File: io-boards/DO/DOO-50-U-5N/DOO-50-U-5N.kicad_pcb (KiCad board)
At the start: 2 copper layers, 50 x 33 mm, 17 parts, among them J1 GPP_Conn_01x12_Pin, J3 Conn_01x02_Socket, J4 Conn_01x02_Socket, Q1 NDT3055L, Q2 BC807, U1 PC817

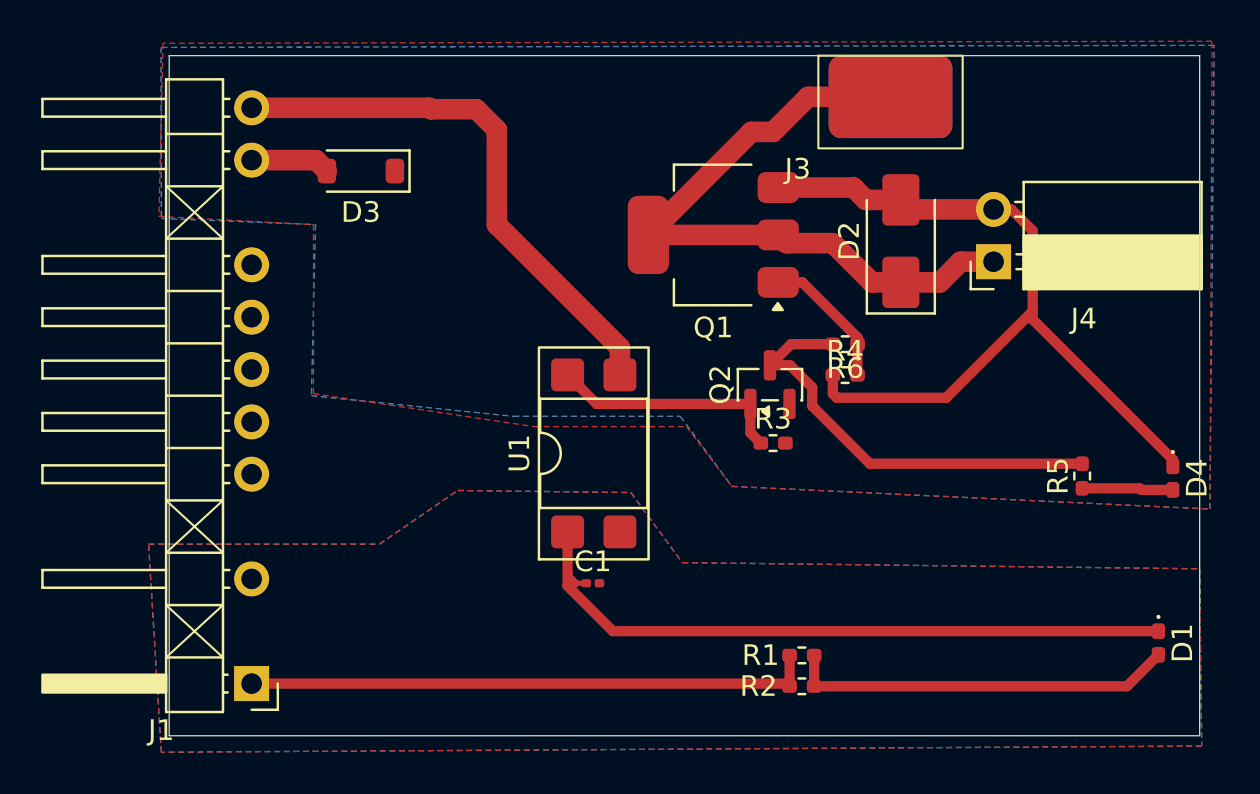
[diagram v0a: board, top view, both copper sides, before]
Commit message: Made some corrections after assembling of prototype PCBs
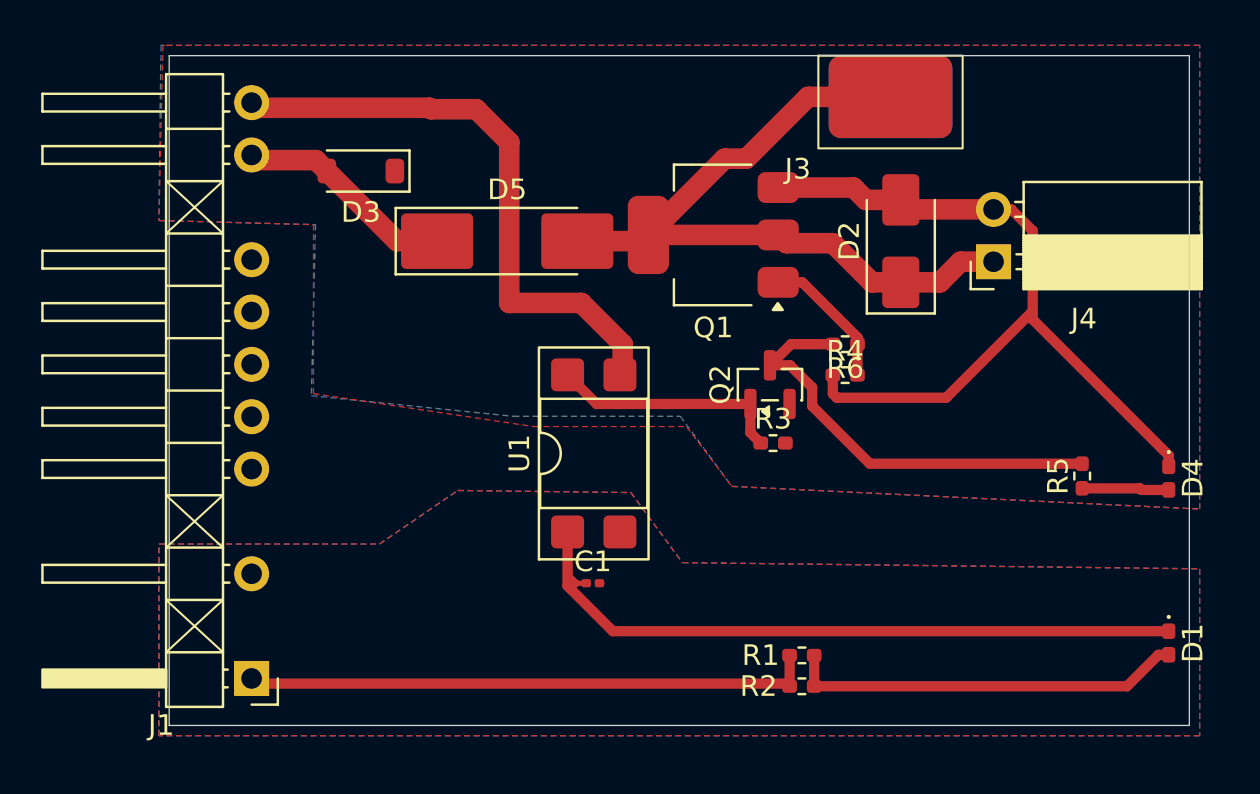
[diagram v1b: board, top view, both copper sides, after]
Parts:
- added D5: SM4007, Diode_SMD:D_MELF_Handsoldering, F.Cu at (116.4, 59.0)
- moved D1 0.50 mm to (148.5, 78.5)
- moved J1 0.25 mm to (104.0, 80.2)
- moved D4 0.20 mm to (148.5, 70.5)
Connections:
- net Net-(D3-A) renamed fly
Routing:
- net fly: track 3.87 -> 10.6 mm
- net Net-(D2-A1): track 32.6 -> 36.2 mm
- net GND1: track 66.6 -> 68.7 mm
- net Net-(D1-K): track 36.2 -> 36.7 mm
- net Net-(D1-A): track 18.8 -> 19.3 mm
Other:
- board size 50 x 33 mm -> 49.5 x 32.5 mm
